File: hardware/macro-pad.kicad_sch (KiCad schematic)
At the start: 41 parts, among them J1 USB_C_Receptacle_USB2.0, SW1 PEC12R-4025F-S0024, SW2 MX1A-G1NA, SW3 MX1A-G1NA, SW4 MX1A-G1NA, SW5 MX1A-G1NA, U1 MIC5317-3.3ZD5-TR, U2 RP2040, U3 W25Q128JVSIQ, Y1 ABLS-12.000MHZ-B4-T

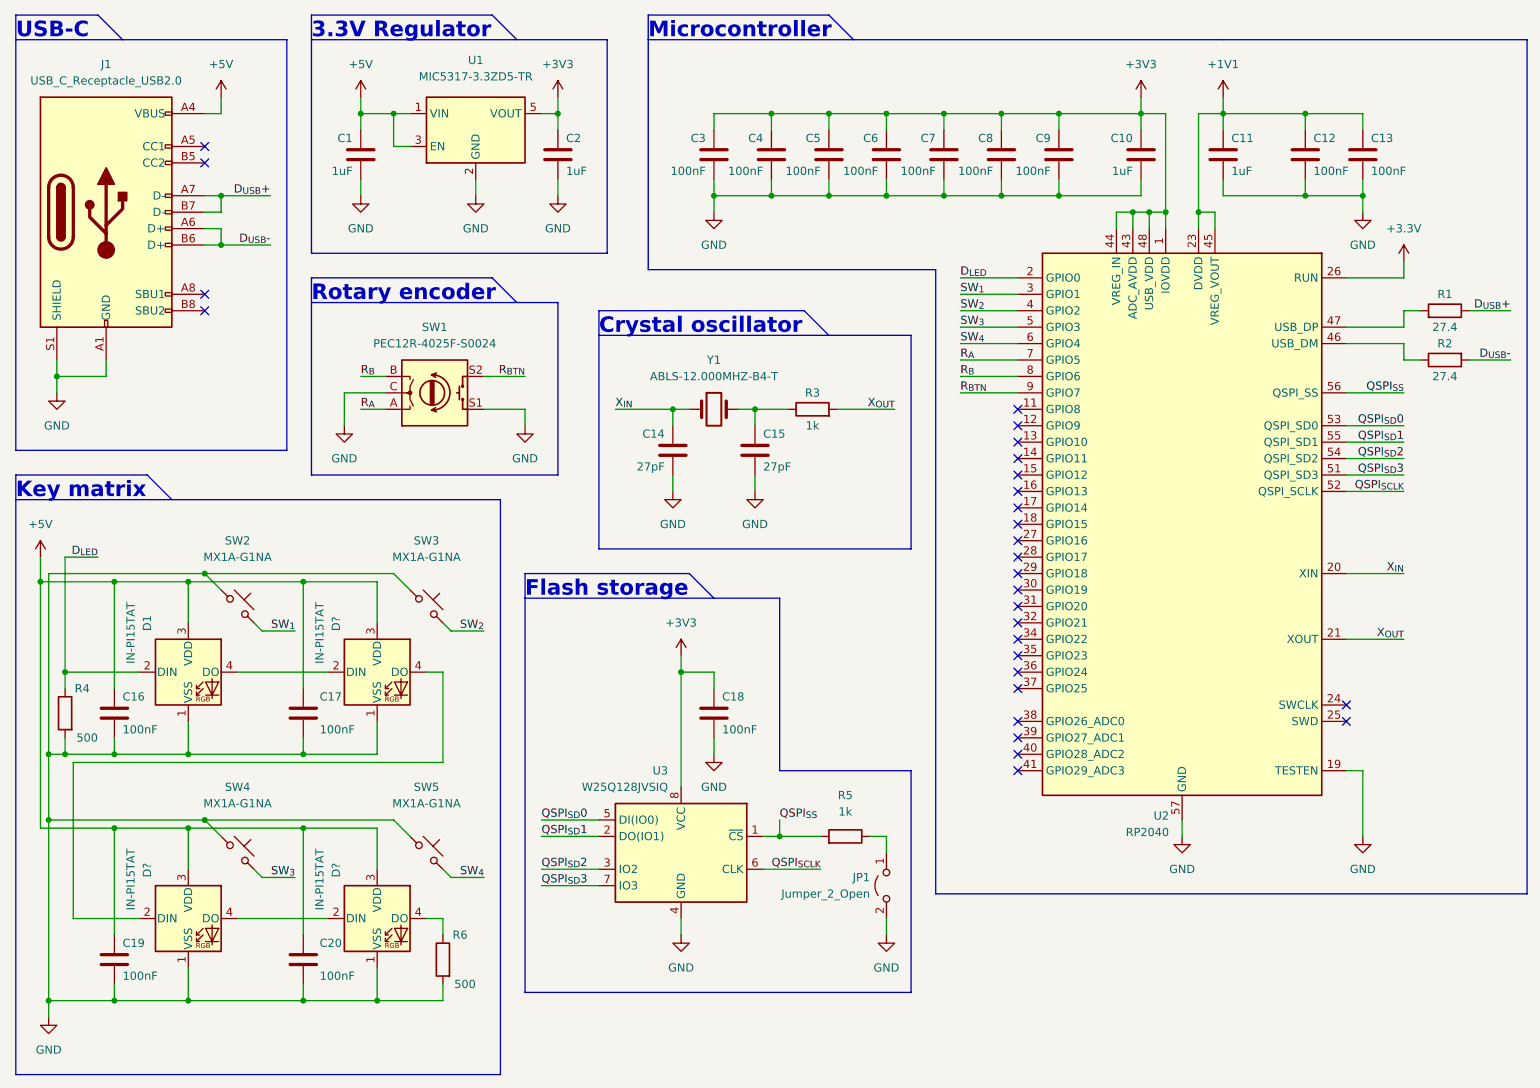
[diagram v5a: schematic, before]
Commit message: Fixed invlid 3.3V flag
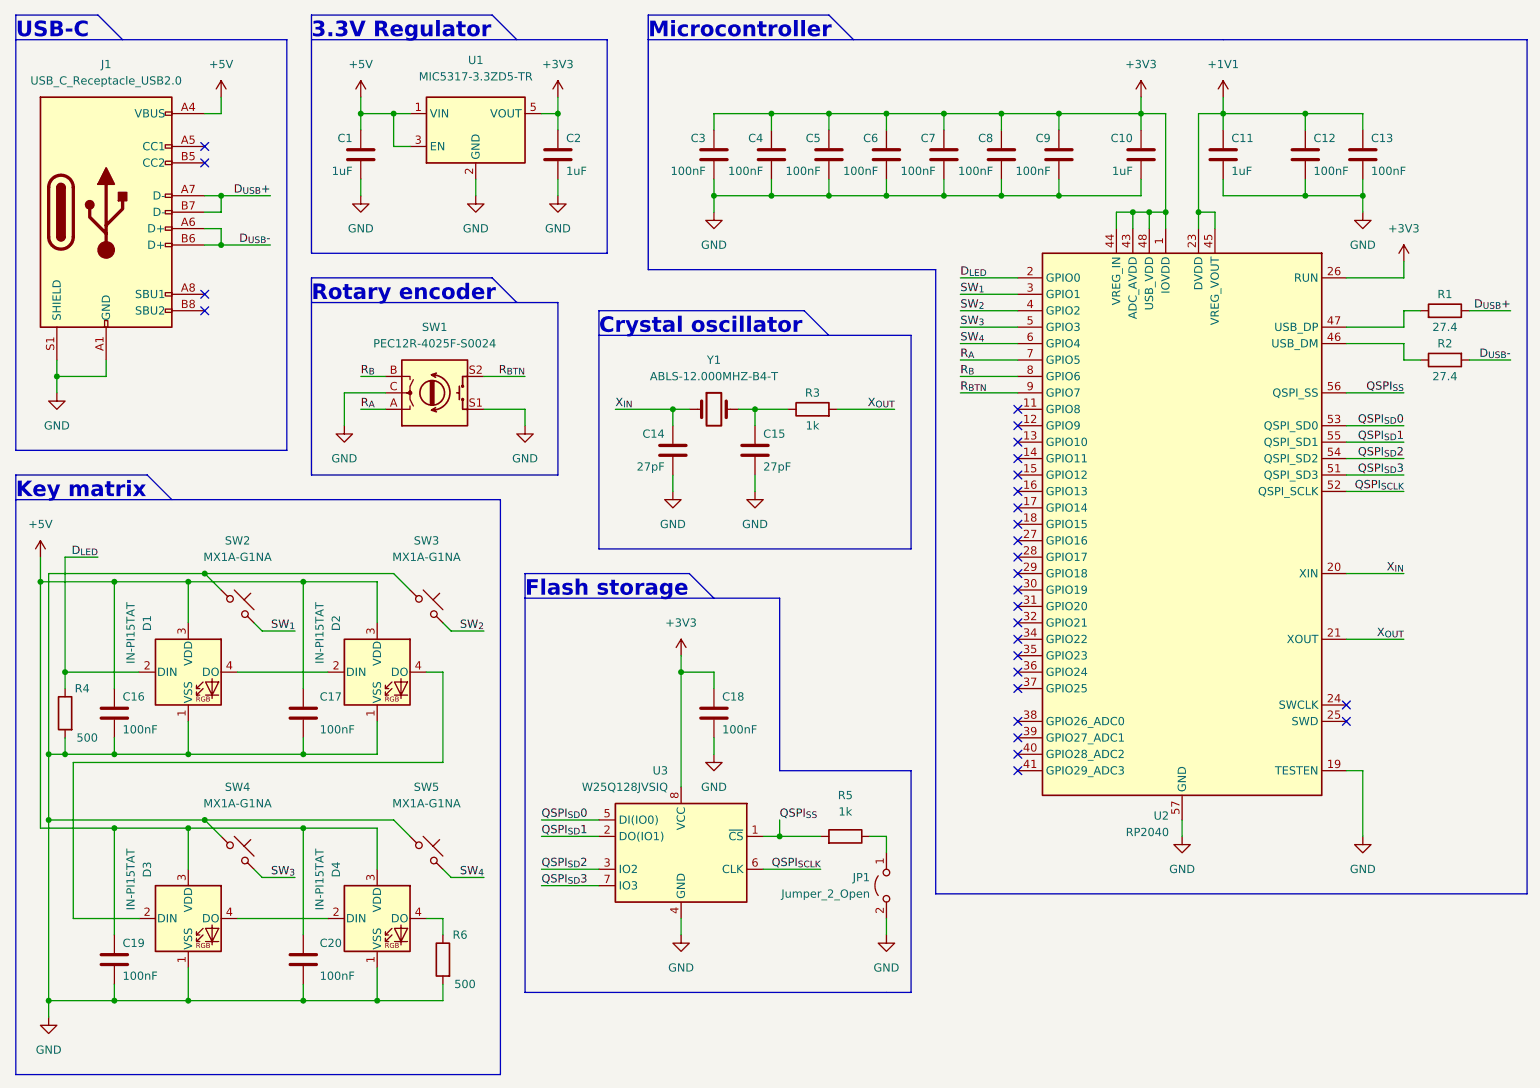
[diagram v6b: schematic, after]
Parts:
- gave numbers to parts that had none: 3
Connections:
- net +3.3V is gone; now on net +3V3: U2.26 (RUN)
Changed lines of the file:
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@@
   (symbol (lib_id "LED:Inolux_IN-PI554FCH") (at 81.28 161.29 0) (unit 1)
     (in_bom yes) (on_board yes)
-    (property "Reference" "D?" (id 0) (at 74.93 154.94 90)
+    (property "Reference" "D4" (id 0) (at 74.93 154.94 90)
       (effects (font (size 1.27 1.27)) (justify left))
     )
@@
   (symbol (lib_id "power:+3V3") (at 128.27 120.65 0) (mirror y) (unit 1)
     (in_bom yes) (on_board yes) (fields_autoplaced)
-    (property "Reference" "#PWR019" (id 0) (at 128.27 124.46 0)
+    (property "Reference" "#PWR018" (id 0) (at 128.27 124.46 0)
       (effects (font (size 1.27 1.27)) hide)
     )
@@
   (symbol (lib_id "power:GND") (at 76.2 85.09 0) (unit 1)
     (in_bom yes) (on_board yes) (fields_autoplaced)
-    (property "Reference" "#PWR0102" (id 0) (at 76.2 91.44 0)
+    (property "Reference" "#PWR013" (id 0) (at 76.2 91.44 0)
       (effects (font (size 1.27 1.27)) hide)
     )
@@
   (symbol (lib_id "power:GND") (at 104.14 85.09 0) (unit 1)
     (in_bom yes) (on_board yes) (fields_autoplaced)
-    (property "Reference" "#PWR0101" (id 0) (at 104.14 91.44 0)
+    (property "Reference" "#PWR014" (id 0) (at 104.14 91.44 0)
       (effects (font (size 1.27 1.27)) hide)
     )
@@
   (symbol (lib_id "power:GND") (at 160.02 163.83 0) (mirror y) (unit 1)
     (in_bom yes) (on_board yes) (fields_autoplaced)
-    (property "Reference" "#PWR024" (id 0) (at 160.02 170.18 0)
+    (property "Reference" "#PWR023" (id 0) (at 160.02 170.18 0)
       (effects (font (size 1.27 1.27)) hide)
     )
@@
   (symbol (lib_id "power:GND") (at 205.74 148.59 0) (mirror y) (unit 1)
     (in_bom yes) (on_board yes) (fields_autoplaced)
-    (property "Reference" "#PWR021" (id 0) (at 205.74 154.94 0)
+    (property "Reference" "#PWR020" (id 0) (at 205.74 154.94 0)
       (effects (font (size 1.27 1.27)) hide)
     )
@@
     (pin "2")
   )
+  (symbol (lib_id "power:+3V3") (at 240.03 59.69 0) (mirror y) (unit 1)
+    (in_bom yes) (on_board yes) (fields_autoplaced)
+    (property "Reference" "#PWR?" (id 0) (at 240.03 63.5 0)
+      (effects (font (size 1.27 1.27)) hide)
+    )
+    (property "Value" "+3V3" (id 1) (at 240.03 54.61 0))
+    (property "Footprint" "" (id 2) (at 240.03 59.69 0)
+      (effects (font (size 1.27 1.27)) hide)
+    )
+    (property "Datasheet" "" (id 3) (at 240.03 59.69 0)
+      (effects (font (size 1.27 1.27)) hide)
+    )
+    (pin "1")
+  )
   (symbol (lib_id "power:GND") (at 233.68 148.59 0) (mirror y) (unit 1)
     (in_bom yes) (on_board yes) (fields_autoplaced)
-    (property "Reference" "#PWR022" (id 0) (at 233.68 154.94 0)
+    (property "Reference" "#PWR021" (id 0) (at 233.68 154.94 0)
       (effects (font (size 1.27 1.27)) hide)
     )
@@
   (symbol (lib_id "power:GND") (at 128.27 163.83 0) (mirror y) (unit 1)
     (in_bom yes) (on_board yes) (fields_autoplaced)
-    (property "Reference" "#PWR023" (id 0) (at 128.27 170.18 0)
+    (property "Reference" "#PWR022" (id 0) (at 128.27 170.18 0)
       (effects (font (size 1.27 1.27)) hide)
     )
@@
   (symbol (lib_id "power:GND") (at 30.48 176.53 0) (unit 1)
     (in_bom yes) (on_board yes) (fields_autoplaced)
-    (property "Reference" "#PWR025" (id 0) (at 30.48 182.88 0)
+    (property "Reference" "#PWR024" (id 0) (at 30.48 182.88 0)
       (effects (font (size 1.27 1.27)) hide)
     )
@@
     (pin "1")
   )
-  (symbol (lib_id "power:+3.3V") (at 240.03 59.69 0) (mirror y) (unit 1)
-    (in_bom yes) (on_board yes) (fields_autoplaced)
-    (property "Reference" "#PWR011" (id 0) (at 240.03 63.5 0)
-      (effects (font (size 1.27 1.27)) hide)
-    )
-    (property "Value" "+3.3V" (id 1) (at 240.03 54.61 0))
-    (property "Footprint" "" (id 2) (at 240.03 59.69 0)
-      (effects (font (size 1.27 1.27)) hide)
-    )
-    (property "Datasheet" "" (id 3) (at 240.03 59.69 0)
-      (effects (font (size 1.27 1.27)) hide)
-    )
-    (pin "1")
-  )
   (symbol (lib_id "Device:C") (at 78.74 43.18 0) (mirror y) (unit 1)
     (in_bom yes) (on_board yes)
@@
   (symbol (lib_id "power:GND") (at 133.35 135.89 0) (mirror y) (unit 1)
     (in_bom yes) (on_board yes)
-    (property "Reference" "#PWR020" (id 0) (at 133.35 142.24 0)
+    (property "Reference" "#PWR019" (id 0) (at 133.35 142.24 0)
       (effects (font (size 1.27 1.27)) hide)
     )
@@
   (symbol (lib_id "LED:Inolux_IN-PI554FCH") (at 81.28 123.19 0) (unit 1)
     (in_bom yes) (on_board yes)
-    (property "Reference" "D?" (id 0) (at 74.93 116.84 90)
+    (property "Reference" "D2" (id 0) (at 74.93 116.84 90)
       (effects (font (size 1.27 1.27)) (justify left))
     )
@@
   (symbol (lib_id "power:GND") (at 31.75 80.01 0) (unit 1)
     (in_bom yes) (on_board yes) (fields_autoplaced)
-    (property "Reference" "#PWR014" (id 0) (at 31.75 86.36 0)
+    (property "Reference" "#PWR012" (id 0) (at 31.75 86.36 0)
       (effects (font (size 1.27 1.27)) hide)
     )
@@
   (symbol (lib_id "LED:Inolux_IN-PI554FCH") (at 52.07 161.29 0) (unit 1)
     (in_bom yes) (on_board yes)
-    (property "Reference" "D?" (id 0) (at 45.72 154.94 90)
+    (property "Reference" "D3" (id 0) (at 45.72 154.94 90)
       (effects (font (size 1.27 1.27)) (justify left))
     )
@@
       (reference "#PWR010") (unit 1) (value "GND") (footprint "")
     )
-    (path "/cf8b9d0f-0980-41d9-bcff-123b3899245a"
-      (reference "#PWR011") (unit 1) (value "+3.3V") (footprint "")
-    )
     (path "/e03294de-26b7-4ff0-85aa-3b23c9e1d17d"
+      (reference "#PWR012") (unit 1) (value "GND") (footprint "")
+    )
+    (path "/62c929bd-6f26-4578-bfff-98f3c42f1083"
+      (reference "#PWR013") (unit 1) (value "GND") (footprint "")
+    )
+    (path "/71ca22fd-6f1e-4536-87f9-d0864b125d1d"
       (reference "#PWR014") (unit 1) (value "GND") (footprint "")
     )
@@
     )
     (path "/35b717b2-41f7-4473-871b-bd82403ccf49"
-      (reference "#PWR019") (unit 1) (value "+3V3") (footprint "")
+      (reference "#PWR018") (unit 1) (value "+3V3") (footprint "")
     )
     (path "/d7e1e858-d128-42ad-9e5f-d91eae131525"
+      (reference "#PWR019") (unit 1) (value "GND") (footprint "")
+    )
+    (path "/a6c652f8-8566-4182-97f5-b5f07b2ffa2a"
       (reference "#PWR020") (unit 1) (value "GND") (footprint "")
     )
-    (path "/a6c652f8-8566-4182-97f5-b5f07b2ffa2a"
+    (path "/ae1668cc-cfe8-4494-a741-fe2db7dad924"
       (reference "#PWR021") (unit 1) (value "GND") (footprint "")
     )
-    (path "/ae1668cc-cfe8-4494-a741-fe2db7dad924"
+    (path "/c1a7cb41-542e-46af-a46e-09d74eab5343"
       (reference "#PWR022") (unit 1) (value "GND") (footprint "")
     )
-    (path "/c1a7cb41-542e-46af-a46e-09d74eab5343"
+    (path "/a03f6cf3-c1f3-44ac-93b4-0e000a1ffa32"
       (reference "#PWR023") (unit 1) (value "GND") (footprint "")
     )
-    (path "/a03f6cf3-c1f3-44ac-93b4-0e000a1ffa32"
+    (path "/c3427917-2fcc-4da9-950a-66a0b821fc50"
       (reference "#PWR024") (unit 1) (value "GND") (footprint "")
     )
-    (path "/c3427917-2fcc-4da9-950a-66a0b821fc50"
-      (reference "#PWR025") (unit 1) (value "GND") (footprint "")
-    )
-    (path "/71ca22fd-6f1e-4536-87f9-d0864b125d1d"
-      (reference "#PWR0101") (unit 1) (value "GND") (footprint "")
-    )
-    (path "/62c929bd-6f26-4578-bfff-98f3c42f1083"
-      (reference "#PWR0102") (unit 1) (value "GND") (footprint "")
+    (path "/adb6811a-a9a8-4834-8611-3e456e25cf80"
+      (reference "#PWR?") (unit 1) (value "+3V3") (footprint "")
     )
     (path "/d3290334-df8d-42fb-8f84-c8b579cd4c2d"
@@
       (reference "D1") (unit 1) (value "IN-PI15TAT") (footprint "LED_SMD:LED_SK6812_EC15_1.5x1.5mm")
     )
+    (path "/d9d2ab8e-70af-4edc-af85-5bd08e252126"
+      (reference "D2") (unit 1) (value "IN-PI15TAT") (footprint "LED_SMD:LED_SK6812_EC15_1.5x1.5mm")
+    )
+    (path "/f7546c84-0c42-45d8-95ea-e9b90ba86f3b"
+      (reference "D3") (unit 1) (value "IN-PI15TAT") (footprint "LED_SMD:LED_SK6812_EC15_1.5x1.5mm")
+    )
     (path "/077c08c6-e039-4dcf-b5c9-909d03944414"
-      (reference "D?") (unit 1) (value "IN-PI15TAT") (footprint "LED_SMD:LED_SK6812_EC15_1.5x1.5mm")
-    )
-    (path "/d9d2ab8e-70af-4edc-af85-5bd08e252126"
-      (reference "D?") (unit 1) (value "IN-PI15TAT") (footprint "LED_SMD:LED_SK6812_EC15_1.5x1.5mm")
-    )
-    (path "/f7546c84-0c42-45d8-95ea-e9b90ba86f3b"
-      (reference "D?") (unit 1) (value "IN-PI15TAT") (footprint "LED_SMD:LED_SK6812_EC15_1.5x1.5mm")
+      (reference "D4") (unit 1) (value "IN-PI15TAT") (footprint "LED_SMD:LED_SK6812_EC15_1.5x1.5mm")
     )
     (path "/e325433c-a087-465d-b143-a8822076c064"
